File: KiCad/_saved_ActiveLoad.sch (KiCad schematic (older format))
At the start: 61 parts, among them J1 AuxPower, J2 TWI, J3 PDI, J4 TC74X-3.3, J5 PowerInput, J6 FAN, Q2 BC817, Q3 BD911, Q4 BD136, SW1 SW_SPDT, SW2 SW_SPDT, U1 UA78M33, U2 L78M12, U3 ATXMEGA32E5-AU, U4 LM358, U5 TL081

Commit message: Finishing touches
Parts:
- R20: footprint Resistors_THT:R_Axial_Power_L48.0mm_W12.5mm_P55.88mm -> JPResistors:R_Axial_Power_L48.0mm_W12.5mm_P50.8mm
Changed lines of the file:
@@
 F 0 "R20" V 9080 3400 50  0000 C CNN
 F 1 "0R1" V 9000 3400 50  0000 C CNN
-F 2 "Resistors_THT:R_Axial_Power_L48.0mm_W12.5mm_P55.88mm" V 8930 3400 50  0001 C CNN
+F 2 "JPResistors:R_Axial_Power_L48.0mm_W12.5mm_P50.8mm" V 8930 3400 50  0001 C CNN
 F 3 "" H 9000 3400 50  0001 C CNN
 	1    9000 3400

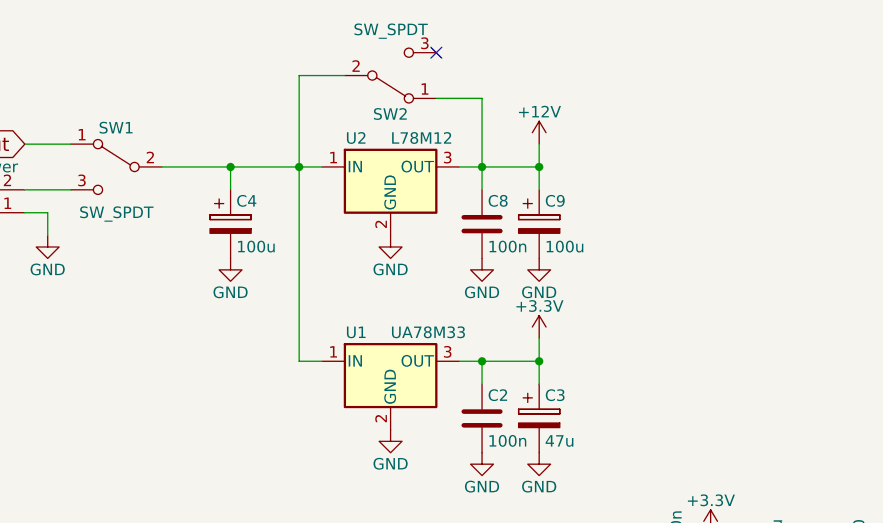
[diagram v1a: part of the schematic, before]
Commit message: Diodes around 7812 added
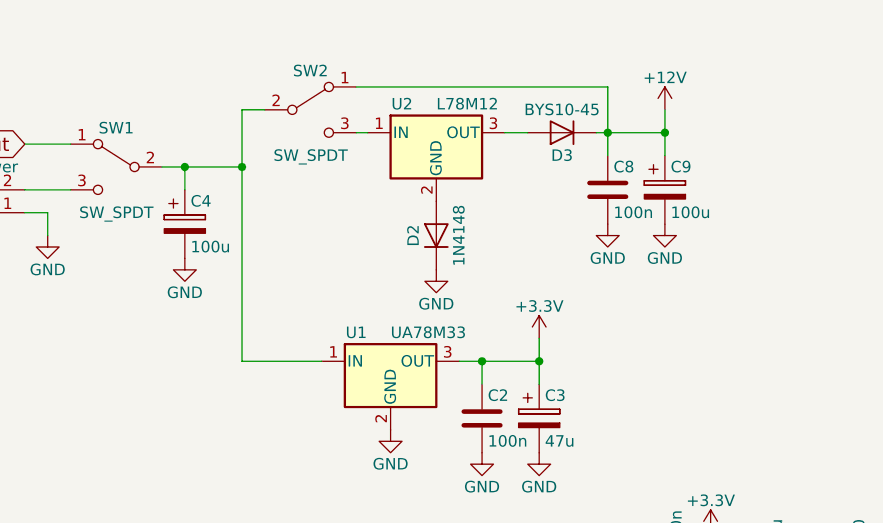
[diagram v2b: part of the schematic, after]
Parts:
- added D2: 1N4148, Diodes_SMD:D_1206, symbol D
- added D3: BYS10-45, Diodes_SMD:D_SMA, symbol D
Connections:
- net +12V: now also D3.1 (K); no longer U2.3 (OUT)
- net GND: now also D2.1 (K); no longer U2.2 (GND)
- net at C4.1, SW1.2 (B), SW2.2 (B)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: no longer U2.1 (IN)
- net at SW2.3 (C): now also U2.1 (IN)
- new net: D2.2 (A), U2.2 (GND)
- new net: D3.2 (A), U2.3 (OUT)
- no-connect marks 5 -> 4
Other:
- moved on the sheet: C4, C8, C9, SW2, U2
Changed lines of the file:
@@
 L L7812 U2
 U 1 1 5AACCCE2
-P 2900 1400
-F 0 "U2" H 2750 1525 50  0000 C CNN
-F 1 "L78M12" H 2900 1525 50  0000 L CNN
-F 2 "TO_SOT_Packages_SMD:TO-252-2_Rectifier" H 2925 1250 50  0001 L CIN
-F 3 "" H 2900 1350 50  0001 C CNN
-	1    2900 1400
+P 3100 1250
+F 0 "U2" H 2950 1375 50  0000 C CNN
+F 1 "L78M12" H 3100 1375 50  0000 L CNN
+F 2 "TO_SOT_Packages_SMD:TO-252-2_Rectifier" H 3125 1100 50  0001 L CIN
+F 3 "" H 3100 1200 50  0001 C CNN
+	1    3100 1250
 	1    0    0    -1
 $EndComp
@@
 L GND #PWR045
 U 1 1 5AACD477
-P 2900 1700
-F 0 "#PWR045" H 2900 1450 50  0001 C CNN
-F 1 "GND" H 2900 1550 50  0000 C CNN
-F 2 "" H 2900 1700 50  0001 C CNN
-F 3 "" H 2900 1700 50  0001 C CNN
-	1    2900 1700
+P 3100 1850
+F 0 "#PWR045" H 3100 1600 50  0001 C CNN
+F 1 "GND" H 3100 1700 50  0000 C CNN
+F 2 "" H 3100 1850 50  0001 C CNN
+F 3 "" H 3100 1850 50  0001 C CNN
+	1    3100 1850
 	1    0    0    -1
 $EndComp
@@
 L C C8
 U 1 1 5AACD983
-P 3300 1650
-F 0 "C8" H 3325 1750 50  0000 L CNN
-F 1 "100n" H 3325 1550 50  0000 L CNN
-F 2 "Capacitors_SMD:C_0805" H 3338 1500 50  0001 C CNN
-F 3 "" H 3300 1650 50  0001 C CNN
-	1    3300 1650
+P 3850 1500
+F 0 "C8" H 3875 1600 50  0000 L CNN
+F 1 "100n" H 3875 1400 50  0000 L CNN
+F 2 "Capacitors_SMD:C_0805" H 3888 1350 50  0001 C CNN
+F 3 "" H 3850 1500 50  0001 C CNN
+	1    3850 1500
 	1    0    0    -1
 $EndComp
@@
 L CP C9
 U 1 1 5AACDA71
-P 3550 1650
-F 0 "C9" H 3575 1750 50  0000 L CNN
-F 1 "100u" H 3575 1550 50  0000 L CNN
-F 2 "Capacitors_SMD:CP_Elec_6.3x7.7" H 3588 1500 50  0001 C CNN
-F 3 "" H 3550 1650 50  0001 C CNN
-	1    3550 1650
+P 4100 1500
+F 0 "C9" H 4125 1600 50  0000 L CNN
+F 1 "100u" H 4125 1400 50  0000 L CNN
+F 2 "Capacitors_SMD:CP_Elec_6.3x7.7" H 4138 1350 50  0001 C CNN
+F 3 "" H 4100 1500 50  0001 C CNN
+	1    4100 1500
 	1    0    0    -1
 $EndComp
@@
 L CP C4
 U 1 1 5AACDB5C
-P 2200 1650
-F 0 "C4" H 2225 1750 50  0000 L CNN
-F 1 "100u" H 2225 1550 50  0000 L CNN
-F 2 "Capacitors_SMD:CP_Elec_6.3x7.7" H 2238 1500 50  0001 C CNN
-F 3 "" H 2200 1650 50  0001 C CNN
-	1    2200 1650
+P 2000 1650
+F 0 "C4" H 2025 1750 50  0000 L CNN
+F 1 "100u" H 2025 1550 50  0000 L CNN
+F 2 "Capacitors_SMD:CP_Elec_6.3x7.7" H 2038 1500 50  0001 C CNN
+F 3 "" H 2000 1650 50  0001 C CNN
+	1    2000 1650
 	1    0    0    -1
 $EndComp
@@
 L GND #PWR046
 U 1 1 5AACDC4E
-P 2200 1800
-F 0 "#PWR046" H 2200 1550 50  0001 C CNN
-F 1 "GND" H 2200 1650 50  0000 C CNN
-F 2 "" H 2200 1800 50  0001 C CNN
-F 3 "" H 2200 1800 50  0001 C CNN
-	1    2200 1800
+P 2000 1800
+F 0 "#PWR046" H 2000 1550 50  0001 C CNN
+F 1 "GND" H 2000 1650 50  0000 C CNN
+F 2 "" H 2000 1800 50  0001 C CNN
+F 3 "" H 2000 1800 50  0001 C CNN
+	1    2000 1800
 	1    0    0    -1
 $EndComp
@@
 L GND #PWR047
 U 1 1 5AACDD19
-P 3300 1800
-F 0 "#PWR047" H 3300 1550 50  0001 C CNN
-F 1 "GND" H 3300 1650 50  0000 C CNN
-F 2 "" H 3300 1800 50  0001 C CNN
-F 3 "" H 3300 1800 50  0001 C CNN
-	1    3300 1800
+P 3850 1650
+F 0 "#PWR047" H 3850 1400 50  0001 C CNN
+F 1 "GND" H 3850 1500 50  0000 C CNN
+F 2 "" H 3850 1650 50  0001 C CNN
+F 3 "" H 3850 1650 50  0001 C CNN
+	1    3850 1650
 	1    0    0    -1
 $EndComp
@@
 L GND #PWR048
 U 1 1 5AACDDE4
-P 3550 1800
-F 0 "#PWR048" H 3550 1550 50  0001 C CNN
-F 1 "GND" H 3550 1650 50  0000 C CNN
-F 2 "" H 3550 1800 50  0001 C CNN
-F 3 "" H 3550 1800 50  0001 C CNN
-	1    3550 1800
+P 4100 1650
+F 0 "#PWR048" H 4100 1400 50  0001 C CNN
+F 1 "GND" H 4100 1500 50  0000 C CNN
+F 2 "" H 4100 1650 50  0001 C CNN
+F 3 "" H 4100 1650 50  0001 C CNN
+	1    4100 1650
 	1    0    0    -1
 $EndComp
@@
 L +12V #PWR049
 U 1 1 5AACE45F
-P 3550 1300
-F 0 "#PWR049" H 3550 1150 50  0001 C CNN
-F 1 "+12V" H 3550 1440 50  0000 C CNN
-F 2 "" H 3550 1300 50  0001 C CNN
-F 3 "" H 3550 1300 50  0001 C CNN
-	1    3550 1300
+P 4100 1150
+F 0 "#PWR049" H 4100 1000 50  0001 C CNN
+F 1 "+12V" H 4100 1290 50  0000 C CNN
+F 2 "" H 4100 1150 50  0001 C CNN
+F 3 "" H 4100 1150 50  0001 C CNN
+	1    4100 1150
 	1    0    0    -1
 $EndComp
@@
 L SW_SPDT SW2
 U 1 1 5AAE5D74
-P 2900 1000
-F 0 "SW2" H 2900 1170 50  0000 C CNN
-F 1 "SW_SPDT" H 2900 800 50  0000 C CNN
-F 2 "JPConnectors:SlideSwitch3Poles" H 2900 1000 50  0001 C CNN
-F 3 "" H 2900 1000 50  0001 C CNN
-	1    2900 1000
-	1    0    0    1
-$EndComp
-NoConn ~ 3100 900
+P 2550 1150
+F 0 "SW2" H 2550 1320 50  0000 C CNN
+F 1 "SW_SPDT" H 2550 950 50  0000 C CNN
+F 2 "JPConnectors:SlideSwitch3Poles" H 2550 1150 50  0001 C CNN
+F 3 "" H 2550 1150 50  0001 C CNN
+	1    2550 1150
+	1    0    0    -1
+$EndComp
 $Comp
 L L7812 U1
@@
 	1300 1500 1500 1500
 Wire Wire Line
-	2500 1000 2500 2250
-Connection ~ 2500 1400
-Wire Wire Line
-	3200 1400 3550 1400
-Wire Wire Line
-	3550 1300 3550 1500
-Wire Wire Line
-	3300 1100 3300 1500
-Connection ~ 3300 1400
-Wire Wire Line
-	2500 1000 2700 1000
-Wire Wire Line
-	3100 1100 3300 1100
-Connection ~ 3550 1400
+	2250 1150 2250 2250
+Connection ~ 2250 1400
+Wire Wire Line
+	4100 1150 4100 1350
+Connection ~ 3850 1250
+Connection ~ 4100 1250
 Wire Wire Line
 	8950 5050 9050 5050
 Wire Wire Line
 	3200 2250 3550 2250
-Connection ~ 2200 1400
-Wire Wire Line
-	2200 1500 2200 1400
-Wire Wire Line
-	1900 1400 2600 1400
-Wire Wire Line
-	2500 2250 2600 2250
+Connection ~ 2000 1400
+Wire Wire Line
+	2000 1500 2000 1400
+Wire Wire Line
+	1900 1400 2250 1400
+Wire Wire Line
+	2250 2250 2600 2250
 Wire Wire Line
 	10250 5650 10250 5550
@@
 Wire Wire Line
 	5950 5200 5850 5200
+Wire Wire Line
+	2750 1250 2800 1250
+Wire Wire Line
+	2750 1050 3850 1050
+Wire Wire Line
+	3850 1050 3850 1350
+$Comp
+L D D2
+U 1 1 5AC556E6
+P 3100 1700
+F 0 "D2" H 3100 1800 50  0000 C CNN
+F 1 "1N4148" H 3100 1600 50  0000 C CNN
+F 2 "Diodes_SMD:D_1206" H 3100 1700 50  0001 C CNN
+F 3 "" H 3100 1700 50  0001 C CNN
+	1    3100 1700
+	0    -1   -1   0
+$EndComp
+$Comp
+L D D3
+U 1 1 5AC55ED7
+P 3650 1250
+F 0 "D3" H 3650 1350 50  0000 C CNN
+F 1 "BYS10-45" H 3650 1150 50  0000 C CNN
+F 2 "Diodes_SMD:D_SMA" H 3650 1250 50  0001 C CNN
+F 3 "" H 3650 1250 50  0001 C CNN
+	1    3650 1250
+	-1   0    0    1
+$EndComp
+Wire Wire Line
+	2250 1150 2350 1150
+Wire Wire Line
+	3400 1250 3500 1250
+Wire Wire Line
+	3800 1250 4100 1250
 $EndSCHEMATC
